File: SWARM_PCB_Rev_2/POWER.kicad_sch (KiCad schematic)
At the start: 54 parts

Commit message: Add MPNs to BOM and apply PCB DFM fixes for JLCPCB
Schematic: added MPN and Manufacturer properties to 205 references
across all sub-sheets (Murata/Yageo/TI/ST/Hirose/JST etc.).
Fixed dU7 description to match INA823DR (not INA828).

PCB: added via tenting (1540 vias), removed stale auto-placement-area
keepout zones (4 zones), increased annular rings on 482 undersized vias
(0.05mm -> 0.1mm), added 6 fiducial markers (3x F.Cu + 3x B.Cu).

Co-Authored-By: Claude Sonnet 4.6 <noreply@anthropic.com>
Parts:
- bC1: MPN (none) -> GRM21BR61A225KE51L; Manufacturer (none) -> Murata
- bC10, bC16, bC17, bC18, bC19, bC7, bC8, bC9: MPN (none) -> GRM21BR60J226ME15L; Manufacturer (none) -> Murata
- bC11, bC2, bC22, bC23, bC6: MPN (none) -> GRM32ER60J226KE20L; Manufacturer (none) -> Murata
- bC12, bC20: MPN (none) -> GRM188R61A105KA61D; Manufacturer (none) -> Murata
- bC13, bC24, bC3: MPN (none) -> GRM188R71C104KA01D; Manufacturer (none) -> Murata
- bC14, bC21, bC4: MPN (none) -> GRM21BR61A106KE18L; Manufacturer (none) -> Murata
- bC15, bC5: MPN (none) -> GRM21BR71H224KA73L; Manufacturer (none) -> Murata
- bC25: MPN (none) -> GRM188R71H103KA01D; Manufacturer (none) -> Murata
- bD1: MPN (none) -> SMBJ18A; Manufacturer (none) -> Vishay
- bD5: MPN (none) -> SS34-HF; Manufacturer (none) -> Vishay
- bF1: MPN (none) -> 1812L150/24MR; Manufacturer (none) -> Littelfuse
- bJ1: MPN (none) -> XT30PW-M; Manufacturer (none) -> Amass
- bJ2: MPN (none) -> B8B-PH-SM4-TB(LF)(SN); Manufacturer (none) -> JST
- bL1: MPN (none) -> 7447799068; Manufacturer (none) -> Würth Elektronik
- bL2: MPN (none) -> 7447799150; Manufacturer (none) -> Würth Elektronik
- bL3: MPN (none) -> ETQP6M220YGC; Manufacturer (none) -> Panasonic
- bR1, bR6, bR7, bR9: MPN (none) -> RC0603FR-07100KL; Manufacturer (none) -> Yageo
- bR10: MPN (none) -> RC0603FR-07187KL; Manufacturer (none) -> Yageo
- bR11: MPN (none) -> RC0603FR-07182KL; Manufacturer (none) -> Yageo
- bR12, bR13, bR14: MPN (none) -> RC0603FR-0710KL; Manufacturer (none) -> Yageo
- bR15: MPN (none) -> RC0603FR-0784K5L; Manufacturer (none) -> Yageo
- bR2: MPN (none) -> RC0603FR-074K7L; Manufacturer (none) -> Yageo
- bR3: MPN (none) -> RC0603FR-0736KL; Manufacturer (none) -> Yageo
- bR4: MPN (none) -> RC0603FR-0782KL; Manufacturer (none) -> Yageo
- bR5: MPN (none) -> RC0603FR-0743K2L; Manufacturer (none) -> Yageo
- bR8: MPN (none) -> RC0603FR-079K09L; Manufacturer (none) -> Yageo
- bU1, bU2: MPN (none) -> LMR33630ADDA; Manufacturer (none) -> Texas Instruments
- bU3: MPN (none) -> TPS55340RTER; Manufacturer (none) -> Texas Instruments

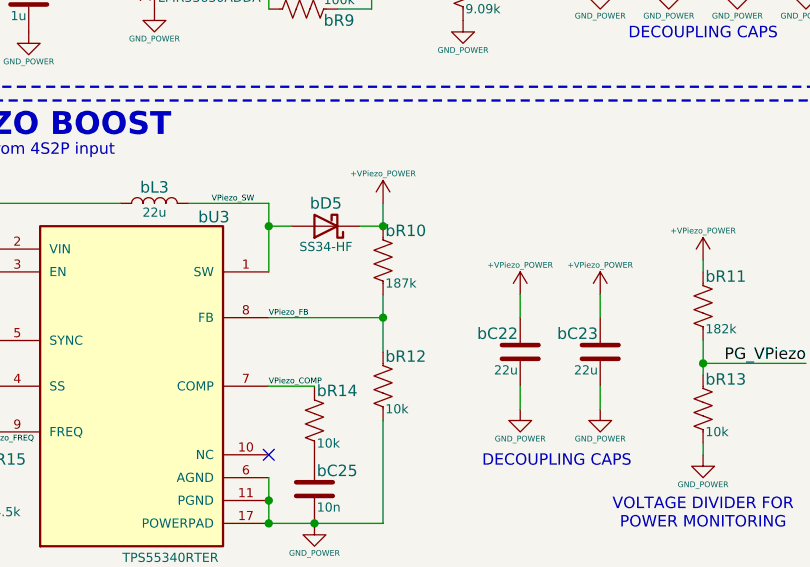
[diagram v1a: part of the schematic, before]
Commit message: Design review fixes: feedback resistor, SWCLK, LED MPNs, GND annotation
- POWER: correct bR10 feedback resistor 187k→255k so TPS55340RTER
  (Vref=0.9V) sets VPiezo to 23.85V (~24V target)
- POWER: assign MPNs for bD2 (green), bD3/bD4 (blue) JE2835 LEDs
- CONTROL: add 33Ω series resistor aR18 on SWCLK near debug header aJ4
- CONTROL: assign MPNs for aD1 (purple) and aD2 (RGB) LEDs
- Top schematic: document isolated GND domain architecture (H3)
- PCB layout, sub-sheet, and SPICE updates

Co-Authored-By: Claude Sonnet 4.6 <noreply@anthropic.com>
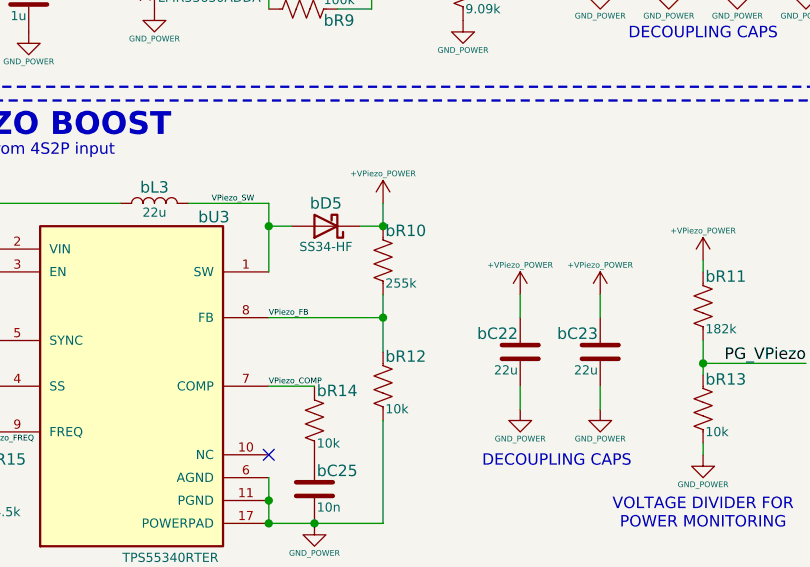
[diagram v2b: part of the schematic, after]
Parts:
- bD2: MP (none) -> JE2835AGR-N-0002A0000-N0000001
- bD3, bD4: MP (none) -> JE2835ABL-N-0005A0000-N0000001
- bR10: value 187k -> 255k

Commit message: Design review fixes: cap voltage ratings, MPN corrections, FET symbol
- POWER: upgrade 17x MLCC MPNs to correct voltage ratings (6.3V/10V caps
  on 12–24V rails replaced with 25V/50V Murata GRM equivalents)
- POWER: fix bR10 MPN to RC0603FR-07255KL (was 187k part, value is 255k)
- CONTROL: fix aR18 MPN to RC0603FR-0733RL (was 10k part, value is 33R)
- TX_RX: replace IPD50R3K0CE lib symbol with Device:MOSFET_N for dQ1-dQ4
- TX_RX: mark dL1/dL2 value as TBD (piezo matching, pending characterisation)
- DESIGN_REVIEW: full review update with all findings by severity

Co-Authored-By: Claude Sonnet 4.6 <noreply@anthropic.com>
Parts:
- bC1: MPN GRM21BR61A225KE51L -> GRM21BR61E225KA73L
- bC10, bC16, bC17, bC18, bC19, bC7, bC8, bC9: MPN GRM21BR60J226ME15L -> GRM21BR61E226ME11L
- bC11, bC2, bC22, bC23, bC6: MPN GRM32ER60J226KE20L -> GRM32ER61H226KE15L
- bC14, bC21, bC4: MPN GRM21BR61A106KE18L -> GRM21BR61E106KA73L
- bR10: MPN RC0603FR-07187KL -> RC0603FR-07255KL
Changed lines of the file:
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@@
 			)
 		)
-		(property "MPN" "GRM21BR60J226ME15L"
+		(property "MPN" "GRM21BR61E226ME11L"
 			(at 0 0 0)
 			(hide yes)
@@
 			)
 		)
-		(property "MPN" "GRM21BR61A106KE18L"
+		(property "MPN" "GRM21BR61E106KA73L"
 			(at 0 0 0)
 			(hide yes)
@@
 			)
 		)
-		(property "MPN" "GRM21BR61A106KE18L"
+		(property "MPN" "GRM21BR61E106KA73L"
 			(at 0 0 0)
 			(hide yes)
@@
 			)
 		)
-		(property "MPN" "GRM21BR60J226ME15L"
+		(property "MPN" "GRM21BR61E226ME11L"
 			(at 0 0 0)
 			(hide yes)
@@
 			)
 		)
-		(property "MPN" "RC0603FR-07187KL"
+		(property "MPN" "RC0603FR-07255KL"
 			(at 0 0 0)
 			(hide yes)
@@
 			)
 		)
-		(property "MPN" "GRM32ER60J226KE20L"
+		(property "MPN" "GRM32ER61H226KE15L"
 			(at 0 0 0)
 			(hide yes)
@@
 			)
 		)
-		(property "MPN" "GRM21BR60J226ME15L"
+		(property "MPN" "GRM21BR61E226ME11L"
 			(at 0 0 0)
 			(hide yes)
@@
 			)
 		)
-		(property "MPN" "GRM21BR60J226ME15L"
+		(property "MPN" "GRM21BR61E226ME11L"
 			(at 0 0 0)
 			(hide yes)
@@
 			)
 		)
-		(property "MPN" "GRM21BR61A225KE51L"
+		(property "MPN" "GRM21BR61E225KA73L"
 			(at 0 0 0)
 			(hide yes)
@@
 			)
 		)
-		(property "MPN" "GRM21BR61A106KE18L"
+		(property "MPN" "GRM21BR61E106KA73L"
 			(at 0 0 0)
 			(hide yes)
@@
 			)
 		)
-		(property "MPN" "GRM21BR60J226ME15L"
+		(property "MPN" "GRM21BR61E226ME11L"
 			(at 0 0 0)
 			(hide yes)
@@
 			)
 		)
-		(property "MPN" "GRM32ER60J226KE20L"
+		(property "MPN" "GRM32ER61H226KE15L"
 			(at 0 0 0)
 			(hide yes)
@@
 			)
 		)
-		(property "MPN" "GRM32ER60J226KE20L"
+		(property "MPN" "GRM32ER61H226KE15L"
 			(at 0 0 0)
 			(hide yes)
@@
 			)
 		)
-		(property "MPN" "GRM32ER60J226KE20L"
+		(property "MPN" "GRM32ER61H226KE15L"
 			(at 0 0 0)
 			(hide yes)
@@
 			)
 		)
-		(property "MPN" "GRM21BR60J226ME15L"
+		(property "MPN" "GRM21BR61E226ME11L"
 			(at 0 0 0)
 			(hide yes)
@@
 			)
 		)
-		(property "MPN" "GRM21BR60J226ME15L"
+		(property "MPN" "GRM21BR61E226ME11L"
 			(at 0 0 0)
 			(hide yes)
@@
 			)
 		)
-		(property "MPN" "GRM21BR60J226ME15L"
+		(property "MPN" "GRM21BR61E226ME11L"
 			(at 0 0 0)
 			(hide yes)
@@
 			)
 		)
-		(property "MPN" "GRM32ER60J226KE20L"
+		(property "MPN" "GRM32ER61H226KE15L"
 			(at 0 0 0)
 			(hide yes)
